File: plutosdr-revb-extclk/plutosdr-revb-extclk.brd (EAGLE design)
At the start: 40 x 40 mm, 30 parts

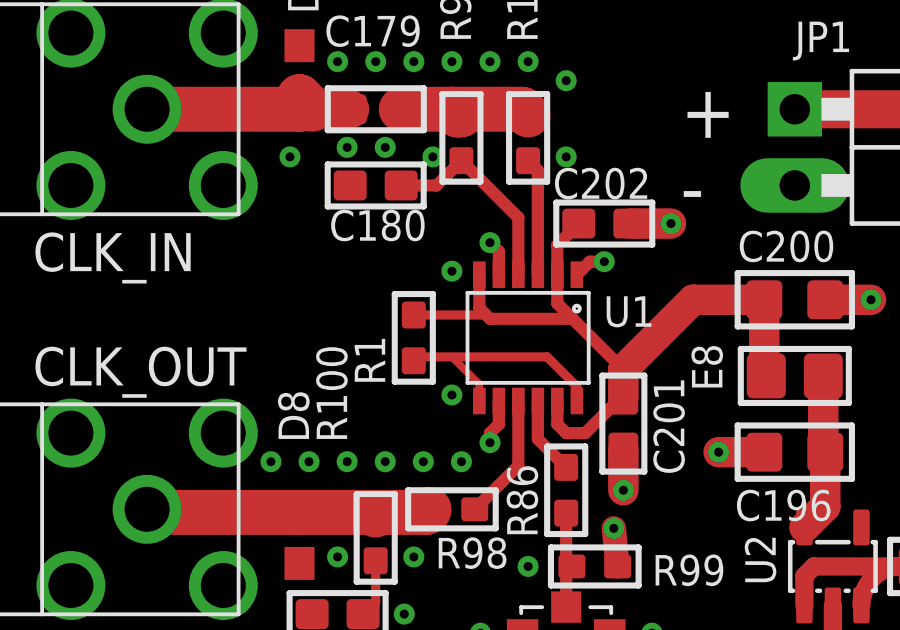
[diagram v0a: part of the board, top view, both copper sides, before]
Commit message: plutosdr-revb-extclk: don't shut-down LTC via SD1/SD2
In the original PlutoSDR RevC or higher, there's a BSS138 FET
that [optionally] pulls low the SD1/SD2 pins in order to activate
the external clock input.

In this circuit, we don't have GPIO control but permanently enable
the LTC.

Related: OS#5892
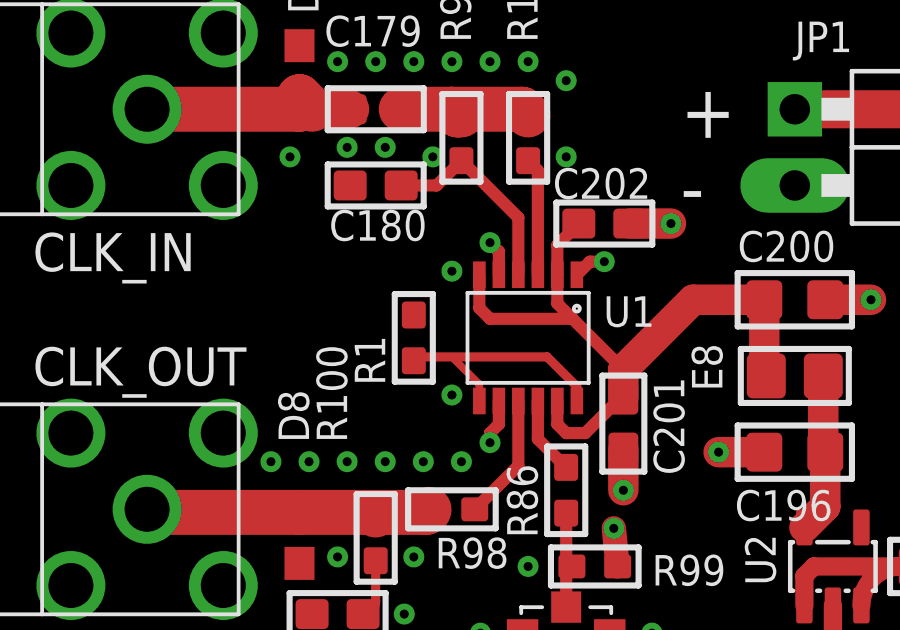
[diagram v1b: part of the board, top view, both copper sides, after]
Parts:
- R1: value 4.7k -> 0
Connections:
- net GND: now also R1.1
- net VCC: no longer R1.1
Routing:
- net VCC: track 25.8 -> 23.4 mm
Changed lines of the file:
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@@
 <attribute name="VALUE" x="12.065" y="11.7475" size="1.27" layer="27" rot="R90"/>
 </element>
-<element name="R1" library="rc-sysmocom" package="_0603" value="4.7k" x="13.97" y="19.05" smashed="yes" rot="R270">
+<element name="R1" library="rc-sysmocom" package="_0603" value="0" x="13.97" y="19.05" smashed="yes" rot="R270">
 <attribute name="NAME" x="13.0175" y="17.4625" size="1.016" layer="25" font="vector" ratio="14" rot="R90"/>
 <attribute name="VALUE" x="12.4777" y="20.6375" size="0.508" layer="27" font="vector" ratio="10" rot="R270"/>
@@
 <via x="15.24" y="21.2725" extent="1-16" drill="0.3"/>
 <via x="15.24" y="17.145" extent="1-16" drill="0.3"/>
+<contactref element="R1" pad="1"/>
 </signal>
 <signal name="N$1">
@@
 <contactref element="U1" pad="2"/>
 <contactref element="U1" pad="11"/>
-<contactref element="R1" pad="1"/>
 <contactref element="E8" pad="2"/>
 <contactref element="C200" pad="2"/>
@@
 <wire x1="16.155" y1="20.04" x2="16.51" y2="19.685" width="0.4064" layer="1"/>
 <wire x1="16.51" y1="19.685" x2="19.265" y2="19.685" width="0.4064" layer="1"/>
-<wire x1="13.97" y1="19.812" x2="16.383" y2="19.812" width="0.3048" layer="1"/>
 <wire x1="16.383" y1="19.812" x2="16.51" y2="19.685" width="0.3048" layer="1"/>
 <wire x1="23.28" y1="20.32" x2="20.955" y2="17.995" width="1.016" layer="1"/>

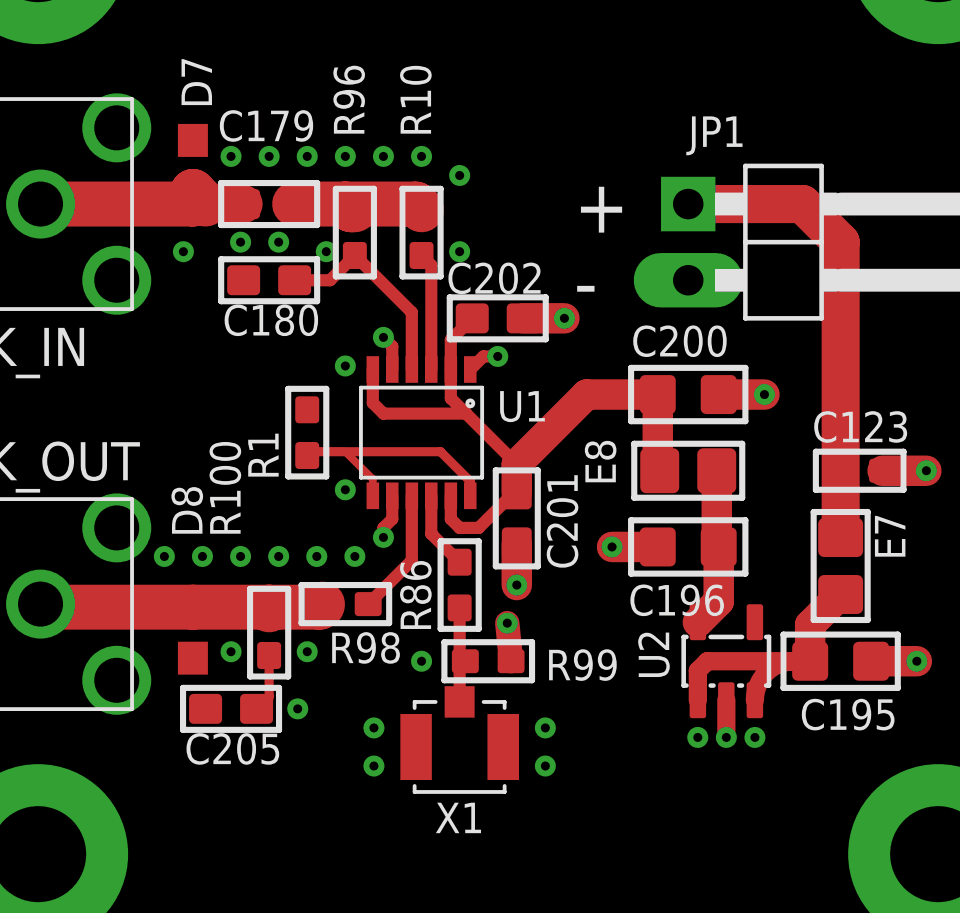
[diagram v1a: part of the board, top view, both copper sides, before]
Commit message: plutosdr-revb-extclk: Fix capacitor footprints
* Always use _0603 and not 0603 (oversized)
* 1uF can be 0603, only 10uF should be 0805

Related: OS#5892
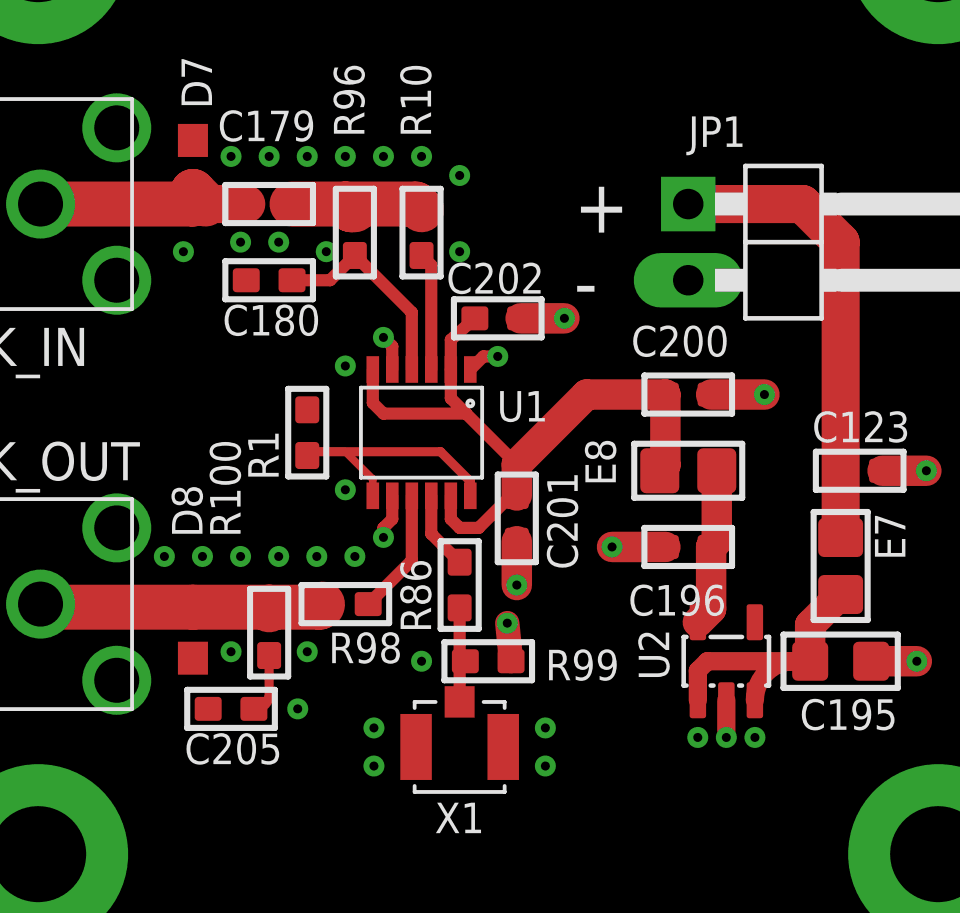
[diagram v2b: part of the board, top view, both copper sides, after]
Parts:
- C179, C180, C201, C202, C205: device rc-sysmocom:0603 -> rc-sysmocom:_0603
- C196, C200: device rc-sysmocom:_0805 -> rc-sysmocom:_0603
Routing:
- net GND: track 15.1 -> 15.8 mm
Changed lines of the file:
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@@
 </autorouter>
 <elements>
-<element name="C179" library="rc-sysmocom" package="0603" value="10n" x="12.7" y="26.67" smashed="yes">
+<element name="C179" library="rc-sysmocom" package="_0603" value="10n" x="12.7" y="26.67" smashed="yes">
 <attribute name="NAME" x="10.9855" y="28.7655" size="1.016" layer="25" font="vector" ratio="14"/>
 <attribute name="VALUE" x="10.9855" y="24.9555" size="0.508" layer="27" font="vector" ratio="10"/>
 </element>
-<element name="C180" library="rc-sysmocom" package="0603" value="10n" x="12.7" y="24.13" smashed="yes">
+<element name="C180" library="rc-sysmocom" package="_0603" value="10n" x="12.7" y="24.13" smashed="yes">
 <attribute name="NAME" x="14.4145" y="23.3045" size="1.016" layer="25" font="vector" ratio="14" rot="R180"/>
 <attribute name="VALUE" x="10.9855" y="22.4155" size="0.508" layer="27" font="vector" ratio="10"/>
 </element>
-<element name="C205" library="rc-sysmocom" package="0603" value="10n" x="11.43" y="9.8425" smashed="yes">
+<element name="C205" library="rc-sysmocom" package="_0603" value="10n" x="11.43" y="9.8425" smashed="yes">
 <attribute name="NAME" x="13.1445" y="9.017" size="1.016" layer="25" font="vector" ratio="14" rot="R180"/>
 <attribute name="VALUE" x="9.7155" y="8.128" size="0.508" layer="27" font="vector" ratio="10"/>
 </element>
-<element name="C201" library="rc-sysmocom" package="0603" value="100n" x="20.955" y="16.1925" smashed="yes" rot="R90">
+<element name="C201" library="rc-sysmocom" package="_0603" value="100n" x="20.955" y="16.1925" smashed="yes" rot="R90">
 <attribute name="NAME" x="22.987" y="14.478" size="1.016" layer="25" font="vector" ratio="14" rot="R90"/>
 <attribute name="VALUE" x="22.6695" y="14.478" size="0.508" layer="27" font="vector" ratio="10" rot="R90"/>
 </element>
-<element name="C202" library="rc-sysmocom" package="0603" value="100n" x="20.32" y="22.86" smashed="yes" rot="R180">
+<element name="C202" library="rc-sysmocom" package="_0603" value="100n" x="20.32" y="22.86" smashed="yes" rot="R180">
 <attribute name="NAME" x="18.6055" y="23.6855" size="1.016" layer="25" font="vector" ratio="14"/>
 <attribute name="VALUE" x="22.0345" y="24.5745" size="0.508" layer="27" font="vector" ratio="10" rot="R180"/>
@@
 <attribute name="VALUE" x="33.9725" y="19.2723" size="0.508" layer="27" font="vector" ratio="10" rot="R180"/>
 </element>
-<element name="C196" library="rc-sysmocom" package="_0805" value="1u" x="26.67" y="15.24" smashed="yes">
+<element name="C196" library="rc-sysmocom" package="_0603" value="1u" x="26.67" y="15.24" smashed="yes">
 <attribute name="NAME" x="27.94" y="13.97" size="1.016" layer="25" font="vector" ratio="14" rot="R180"/>
 <attribute name="VALUE" x="24.7651" y="13.589" size="0.508" layer="27" font="vector" ratio="10"/>
 </element>
-<element name="C200" library="rc-sysmocom" package="_0805" value="1u" x="26.67" y="20.32" smashed="yes" rot="R180">
+<element name="C200" library="rc-sysmocom" package="_0603" value="1u" x="26.67" y="20.32" smashed="yes" rot="R180">
 <attribute name="NAME" x="24.765" y="21.59" size="1.016" layer="25" font="vector" ratio="14"/>
 <attribute name="VALUE" x="28.5749" y="21.971" size="0.508" layer="27" font="vector" ratio="10" rot="R180"/>
@@
 <via x="29.21" y="20.32" extent="1-16" drill="0.3"/>
 <via x="20.955" y="13.97" extent="1-16" drill="0.3"/>
-<wire x1="20.955" y1="15.3425" x2="20.955" y2="13.97" width="1.016" layer="1"/>
+<wire x1="20.955" y1="15.4305" x2="20.955" y2="13.97" width="1.016" layer="1"/>
 <wire x1="16.51" y1="22.225" x2="16.805" y2="21.93" width="0.4064" layer="1"/>
 <wire x1="16.805" y1="21.93" x2="16.805" y2="21.155" width="0.4064" layer="1"/>
@@
 <wire x1="16.805" y1="16.17" x2="16.51" y2="15.875" width="0.4064" layer="1"/>
 <wire x1="16.51" y1="15.875" x2="16.51" y2="15.5575" width="0.4064" layer="1"/>
-<wire x1="27.686" y1="20.32" x2="29.21" y2="20.32" width="1.016" layer="1"/>
+<wire x1="27.432" y1="20.32" x2="29.21" y2="20.32" width="1.016" layer="1"/>
 <via x="34.6075" y="17.78" extent="1-16" drill="0.3"/>
 <via x="34.29" y="11.43" extent="1-16" drill="0.3"/>
@@
 <wire x1="27.94" y1="8.89" x2="27.94" y2="10.13" width="0.6096" layer="1"/>
 <wire x1="32.766" y1="11.43" x2="34.29" y2="11.43" width="1.016" layer="1"/>
-<wire x1="25.654" y1="15.24" x2="24.13" y2="15.24" width="1.016" layer="1"/>
+<wire x1="25.908" y1="15.24" x2="24.13" y2="15.24" width="1.016" layer="1"/>
 <wire x1="33.147" y1="17.78" x2="34.6075" y2="17.78" width="1.016" layer="1"/>
 <wire x1="20.7645" y1="11.43" x2="20.6375" y2="12.7" width="0.8128" layer="1"/>
 <via x="22.5425" y="22.86" extent="1-16" drill="0.3"/>
 <via x="20.32" y="21.59" extent="1-16" drill="0.3"/>
-<wire x1="21.17" y1="22.86" x2="22.5425" y2="22.86" width="1.016" layer="1"/>
+<wire x1="21.082" y1="22.86" x2="22.5425" y2="22.86" width="1.016" layer="1"/>
 <wire x1="20.32" y1="21.59" x2="19.84" y2="21.59" width="0.4064" layer="1"/>
 <wire x1="19.84" y1="21.59" x2="19.405" y2="21.155" width="0.4064" layer="1"/>
@@
 <wire x1="17.455" y1="23.058" x2="15.5575" y2="24.9555" width="0.4064" layer="1"/>
 <wire x1="15.5575" y1="24.9555" x2="14.732" y2="24.13" width="0.4064" layer="1"/>
-<wire x1="14.732" y1="24.13" x2="13.55" y2="24.13" width="0.4064" layer="1"/>
+<wire x1="14.732" y1="24.13" x2="13.462" y2="24.13" width="0.4064" layer="1"/>
 </signal>
 <signal name="VCC">
@@
 <contactref element="C202" pad="2"/>
 <contactref element="C201" pad="2"/>
-<wire x1="25.72" y1="17.78" x2="25.654" y2="17.846" width="1.016" layer="1"/>
-<wire x1="25.654" y1="17.846" x2="25.654" y2="20.32" width="1.016" layer="1"/>
-<wire x1="23.28" y1="20.32" x2="25.654" y2="20.32" width="1.016" layer="1"/>
-<wire x1="19.47" y1="22.86" x2="18.755" y2="22.145" width="0.4064" layer="1"/>
+<wire x1="23.28" y1="20.32" x2="25.908" y2="20.32" width="1.016" layer="1"/>
+<wire x1="19.558" y1="22.86" x2="18.755" y2="22.145" width="0.4064" layer="1"/>
 <wire x1="18.755" y1="22.145" x2="18.755" y2="21.155" width="0.4064" layer="1"/>
 <wire x1="18.755" y1="21.155" x2="18.755" y2="20.195" width="0.4064" layer="1"/>
@@
 <wire x1="16.383" y1="19.812" x2="16.51" y2="19.685" width="0.3048" layer="1"/>
 <wire x1="23.28" y1="20.32" x2="20.955" y2="17.995" width="1.016" layer="1"/>
-<wire x1="20.955" y1="17.995" x2="20.955" y2="17.0425" width="1.016" layer="1"/>
+<wire x1="20.955" y1="17.995" x2="20.955" y2="16.9545" width="1.016" layer="1"/>
 <wire x1="20.955" y1="17.995" x2="19.265" y2="19.685" width="0.4064" layer="1"/>
 <wire x1="18.755" y1="16.945" x2="18.755" y2="16.17" width="0.4064" layer="1"/>
@@
 <wire x1="19.05" y1="15.875" x2="19.685" y2="15.875" width="0.4064" layer="1"/>
 <wire x1="19.685" y1="15.875" x2="20.8525" y2="17.0425" width="0.4064" layer="1"/>
-<wire x1="20.8525" y1="17.0425" x2="20.955" y2="17.0425" width="0.4064" layer="1"/>
+<wire x1="20.8525" y1="17.0425" x2="20.955" y2="16.9545" width="0.4064" layer="1"/>
+<wire x1="25.72" y1="17.78" x2="25.908" y2="17.968" width="1.016" layer="1"/>
+<wire x1="25.908" y1="17.968" x2="25.908" y2="20.32" width="1.016" layer="1"/>
 </signal>
 <signal name="N$7">
@@
 <contactref element="R96" pad="2"/>
 <contactref element="C179" pad="2"/>
-<wire x1="13.55" y1="26.67" x2="15.24" y2="26.67" width="1.5" layer="1"/>
+<wire x1="13.462" y1="26.67" x2="15.24" y2="26.67" width="1.5" layer="1"/>
 <wire x1="15.24" y1="26.67" x2="17.5895" y2="26.67" width="1.5" layer="1"/>
 <wire x1="17.5895" y1="26.67" x2="17.78" y2="26.4795" width="1.5" layer="1"/>
@@
 <contactref element="C205" pad="2"/>
 <wire x1="12.7" y1="11.6205" x2="12.7" y2="10.2625" width="0.3048" layer="1"/>
-<wire x1="12.7" y1="10.2625" x2="12.28" y2="9.8425" width="0.3048" layer="1" curve="-90"/>
+<wire x1="12.7" y1="10.2625" x2="12.192" y2="9.8425" width="0.3048" layer="1" curve="-90"/>
 </signal>
 <signal name="N$10" class="1">
@@
 <wire x1="10.58" y1="26.67" x2="10.16" y2="27.09" width="1.5" layer="1"/>
 <wire x1="5.08" y1="26.67" x2="10.16" y2="26.67" width="1.5" layer="1"/>
-<wire x1="10.58" y1="26.67" x2="11.85" y2="26.67" width="1.27" layer="1"/>
+<wire x1="10.58" y1="26.67" x2="11.938" y2="26.67" width="1.27" layer="1"/>
 <wire x1="10.16" y1="26.67" x2="10.16" y2="27.09" width="1.5" layer="1"/>
 </signal>
@@
 <contactref element="E8" pad="1"/>
 <contactref element="C196" pad="2"/>
-<wire x1="26.99" y1="12.73" x2="27.686" y2="13.426" width="1.016" layer="1"/>
-<wire x1="27.686" y1="13.426" x2="27.686" y2="15.24" width="1.016" layer="1"/>
-<wire x1="27.686" y1="15.24" x2="27.62" y2="15.306" width="1.016" layer="1"/>
-<wire x1="27.62" y1="15.306" x2="27.62" y2="17.78" width="1.016" layer="1"/>
+<wire x1="26.99" y1="12.73" x2="27.432" y2="13.172" width="1.016" layer="1"/>
+<wire x1="27.432" y1="13.172" x2="27.432" y2="15.24" width="1.016" layer="1"/>
+<wire x1="27.432" y1="15.24" x2="27.62" y2="15.428" width="1.016" layer="1"/>
+<wire x1="27.62" y1="15.428" x2="27.62" y2="17.78" width="1.016" layer="1"/>
 </signal>
 </signals>

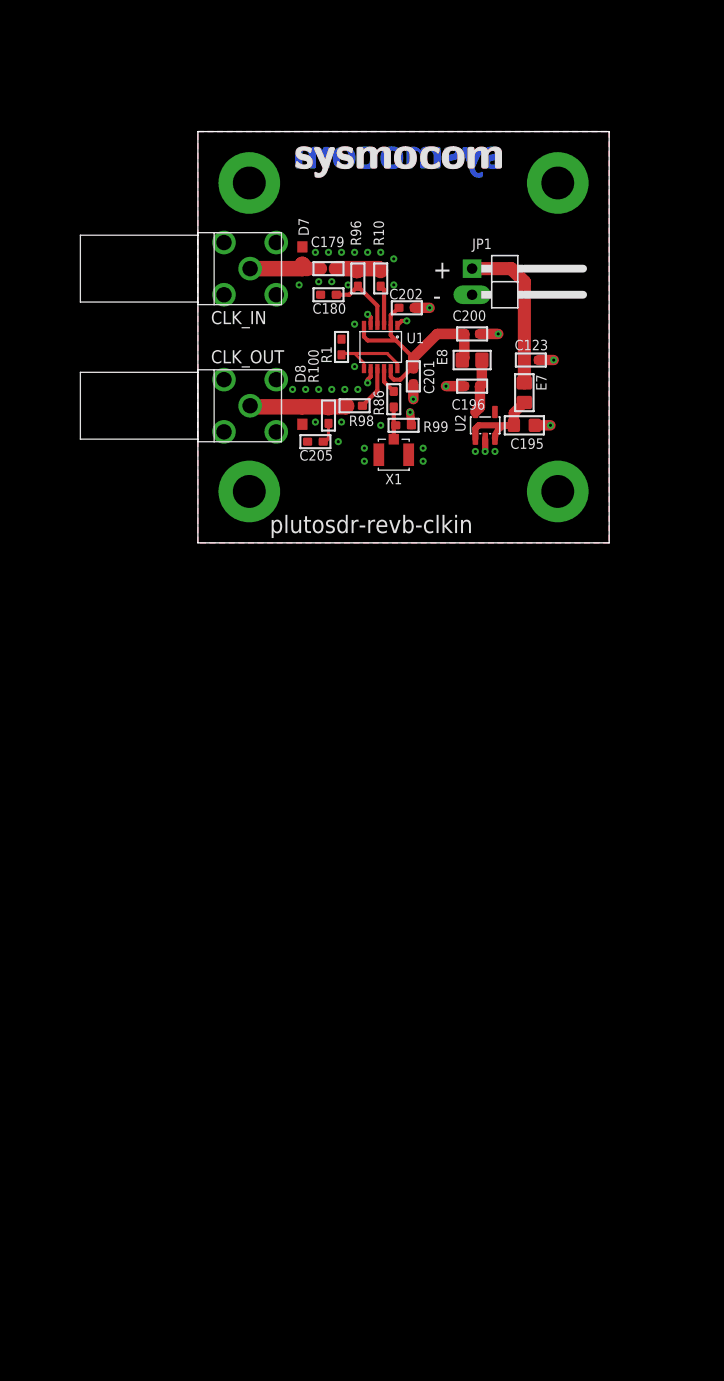
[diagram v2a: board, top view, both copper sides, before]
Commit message: WIP: plutosdr-revb-extclk: support switching back to original 40MHz XO
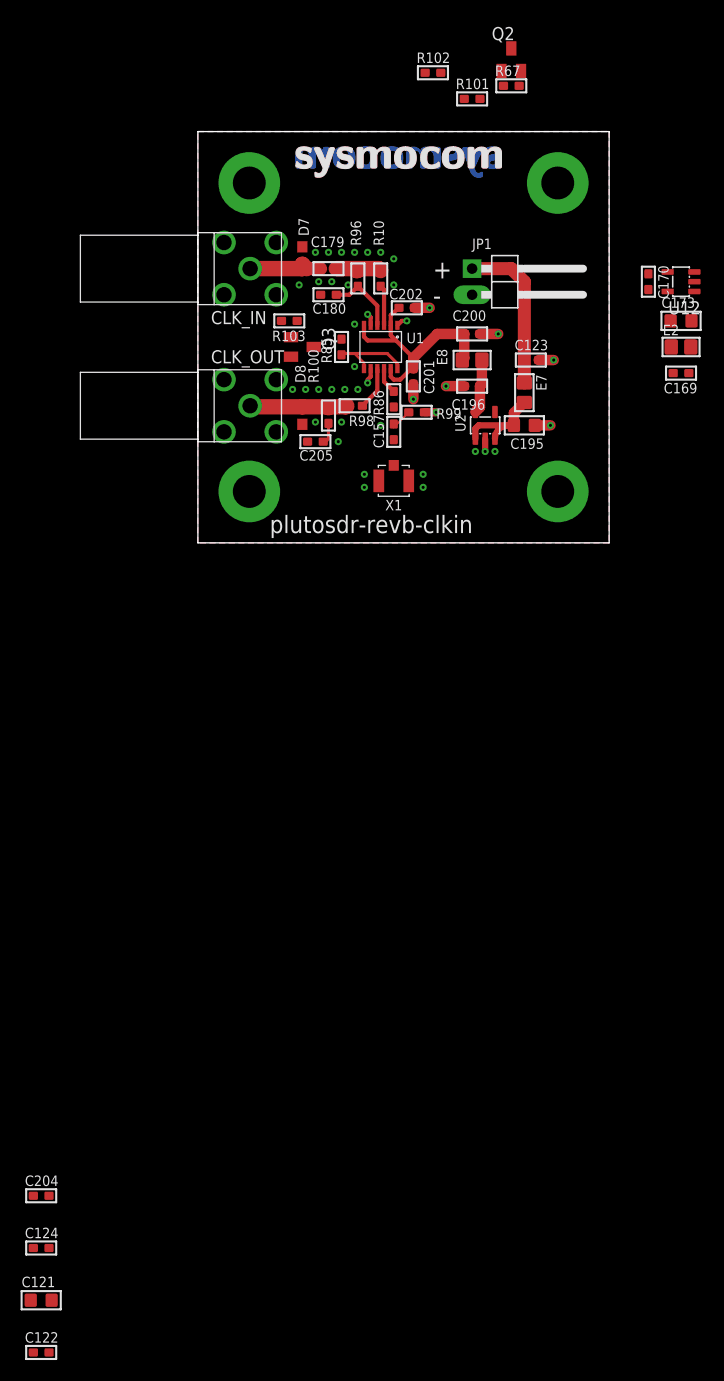
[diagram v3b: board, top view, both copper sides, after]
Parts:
- added C121, C173: 10u, rc-sysmocom:_0805
- added C122: 100n, rc-sysmocom:_0603
- added C124: DNP, rc-sysmocom:_0603
- added C157: 18p, rc-sysmocom:_0603
- added C169, C170: 1u, rc-sysmocom:_0603
- added C204: 47p, rc-sysmocom:_0603
- added E2: 100 OHM, rc-sysmocom:0805
- added Q2, Q3: BSS138, transistor-small-signal:SOT23
- added R101, R103: 2k2, rc-sysmocom:_0603
- added R102: 39, rc-sysmocom:_0603
- added R67: 1k, rc-sysmocom:_0603
- added U12: ADM71670-1.8, ldo:SOT23L
- R85: value 0 -> 4k7
- U2: value (none) -> ADM7160-3.3
- moved X1 2.54 mm to (19.1, 6.03)
- moved R99 1.80 mm to (21.3, 12.7)
- renumbered R1 to R85
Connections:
- new net 1P8V_CLK: C170.2, R101.1, U12.5
- new net CLK_SOURCE_SEL: Q2.1, Q3.1, R102.1, R103.1
- new net N$11: C173.2, E2.2, U12.1, U12.3
- new net N$12: Q2.3, R101.2, R67.2
- new net N$13: R67.1
- new net N$14: C124.2, C204.2
- new net N$15: C204.1
- new net N$16: C157.1, X1.SIG
- new net PS_GPIO6: R102.2
- net 5V_IN: now also C169.2, E2.1
- net GND: now also C169.1, C170.1, C173.1, Q2.2, Q3.2, R103.2, U12.2; no longer R85.1
- net N$1: now also C157.2; no longer X1.SIG
- net N$7: now also Q3.3
- net VCC: now also R85.1
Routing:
- net N$1: track 4.57 -> 2.07 mm
